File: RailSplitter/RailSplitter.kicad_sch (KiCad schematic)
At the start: 24 parts, among them J1 Screw_Terminal_01x02, J2 Screw_Terminal_01x03, Q1 DMP6180SK3, Q2 NJVMJB42CT4G, Q3 NJVMJB41CT4G, U1 OPA990

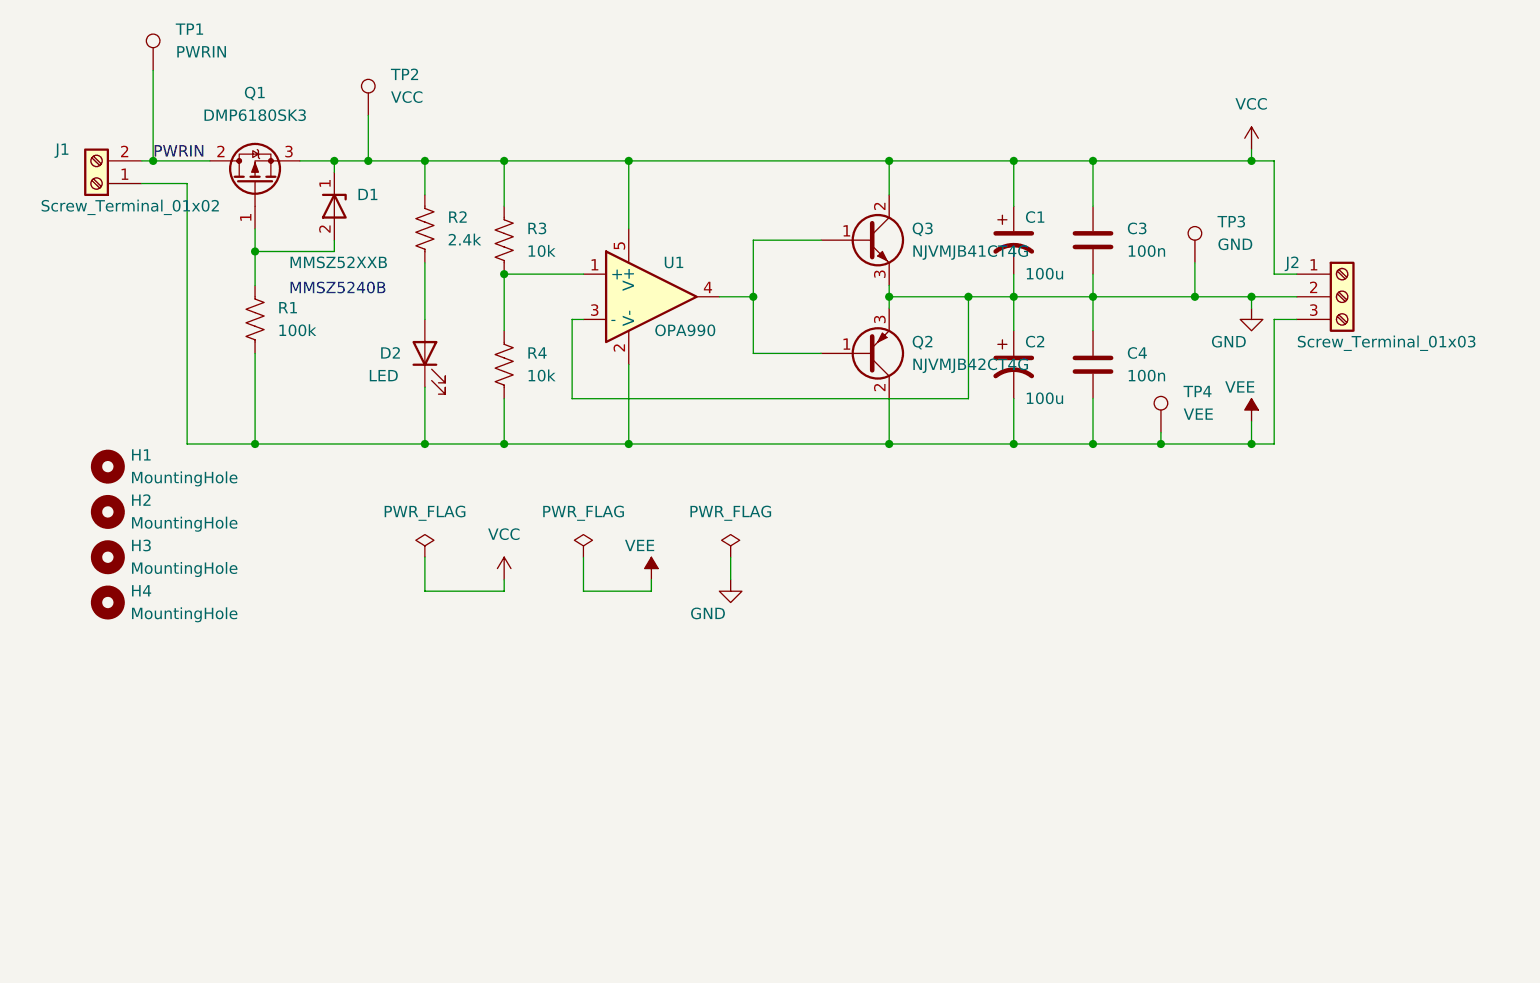
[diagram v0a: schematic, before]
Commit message: Sat: Apr 27 Added Dual H-Bridge Daughterboard and fixed railsplitter
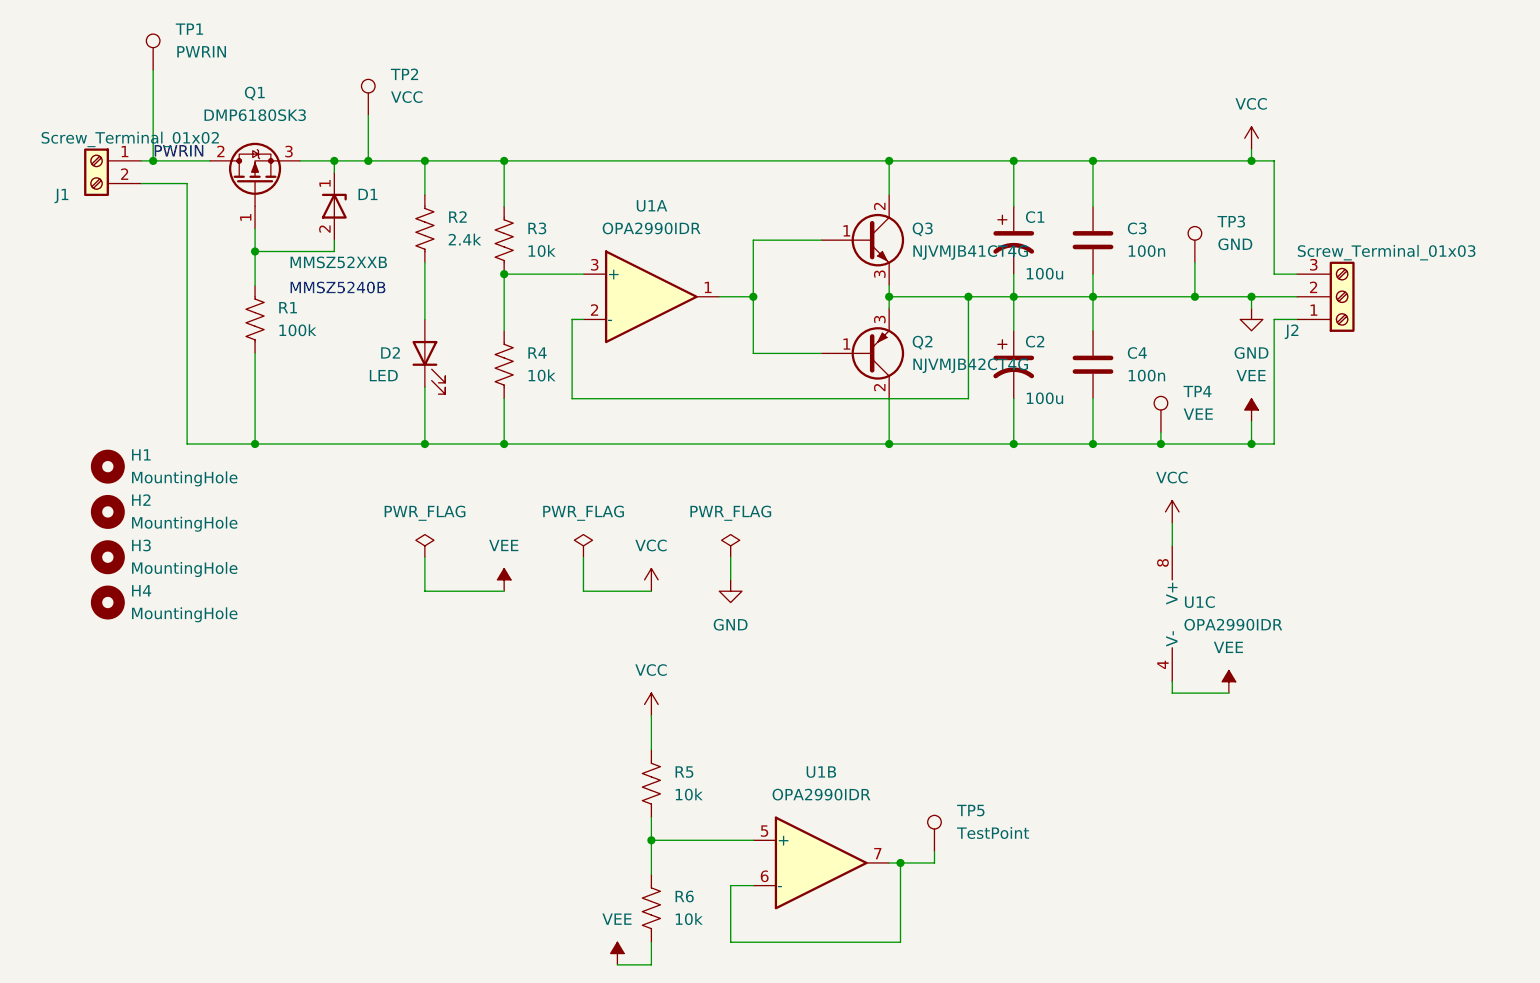
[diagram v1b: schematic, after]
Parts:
- removed U1: OPA990, Package_TO_SOT_SMD:SOT-23-5_HandSoldering, symbol myparts:OPA990
- added R5, R6: 10k, Resistor_SMD:R_1206_3216Metric_Pad1.30x1.75mm_HandSolder, symbol Device:R_US
- added TP5: TestPoint, TestPoint:TestPoint_THTPad_D2.0mm_Drill1.0mm, symbol Connector:TestPoint
- added U1: OPA2990IDR, Package_SO:SOIC-8_3.9x4.9mm_P1.27mm, symbol myparts:OPA2990IDR
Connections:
- net GND: now also U1.2 (-)
- net PWRIN: now also J1.1 (Pin_1); no longer J1.2 (Pin_2)
- net VCC: now also J2.3 (Pin_3), R5.1, U1.8 (V+); no longer J2.1 (Pin_1)
- net VEE: now also J1.2 (Pin_2), J2.1 (Pin_1), R6.2, U1.4 (V-); no longer J1.1 (Pin_1), J2.3 (Pin_3)
- net at R3.2, R4.1: now also U1.3 (+)
- net at Q2.1 (B), Q3.1 (B): now also U1.1
- new net: R5.2, R6.1, U1.5 (+)
- new net: TP5.1, U1.6 (-), U1.7
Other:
- moved on the sheet: J1

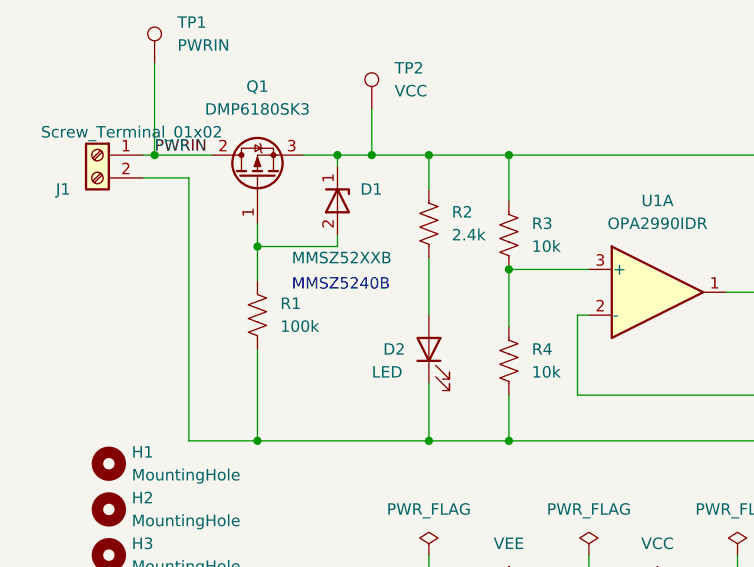
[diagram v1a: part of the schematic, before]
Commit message: created _latest gerber sets and added digikey boms. Also did some project cleanup WedMay82024
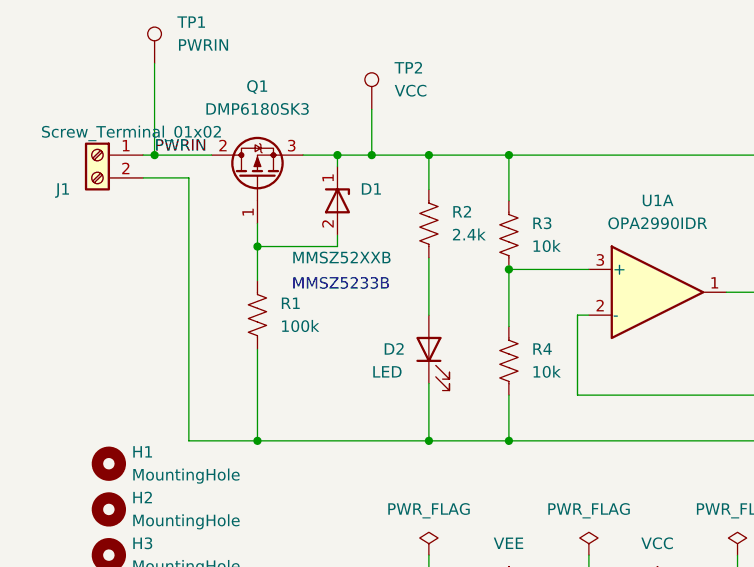
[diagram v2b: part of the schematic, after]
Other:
- note added: "MMSZ5233B"
- note removed: "MMSZ5240B"
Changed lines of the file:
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@@
 		)
 	)
-	(text "MMSZ5240B"
+	(text "MMSZ5233B "
 		(exclude_from_sim no)
 		(at 39.37 85.09 0)
